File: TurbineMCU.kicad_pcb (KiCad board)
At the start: 4 copper layers, 53.7 x 54.7 mm, 44 parts, among them IC1 MSPM0G3507SPMR, IC2 TPS73533DRVT, J1 Conn_01x02_Socket, J10 Conn_01x03_Socket, J13 Conn_01x03_Socket, J14 Conn_01x03_Socket, J15 Conn_01x08_Pin, J2 Conn_01x02_Socket, J3 Conn_01x04_Socket, J5 Conn_01x03_Socket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

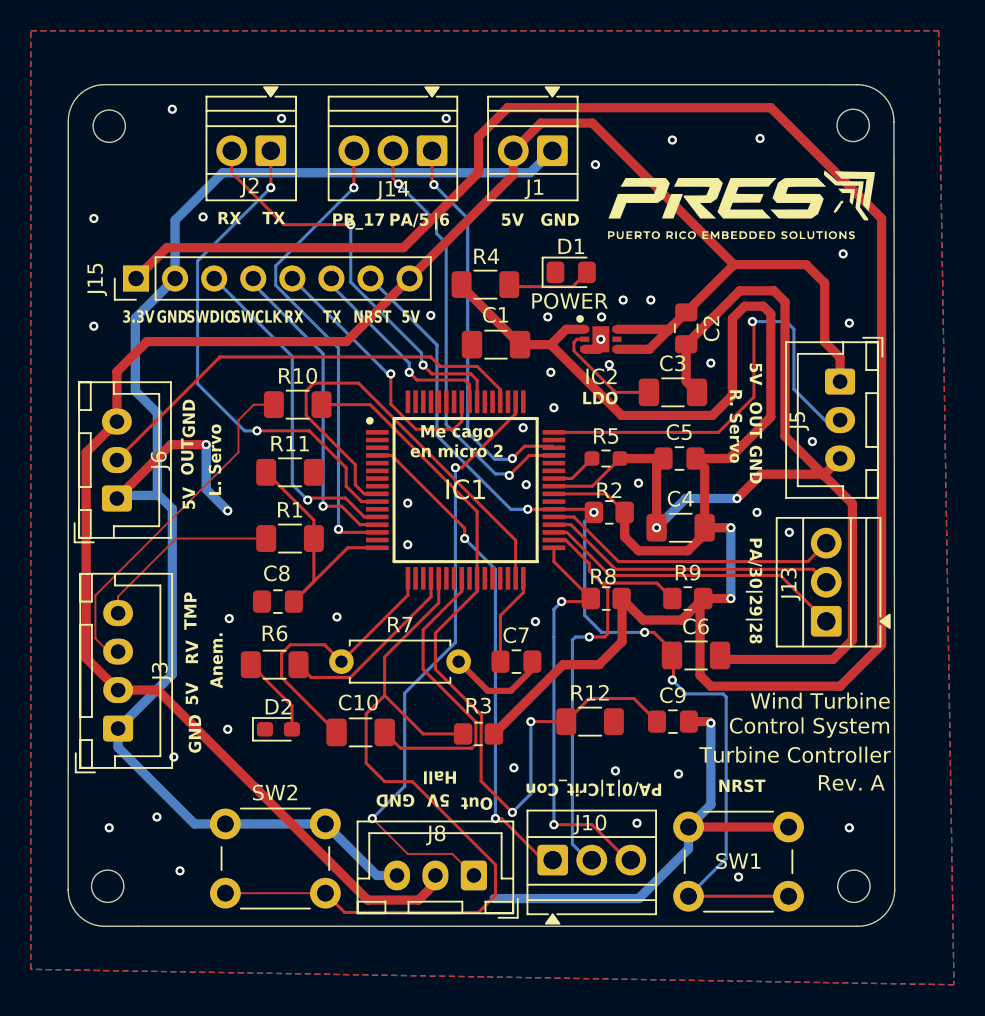
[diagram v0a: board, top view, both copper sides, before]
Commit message: Improved LDO layout based on manufacturer guidelines
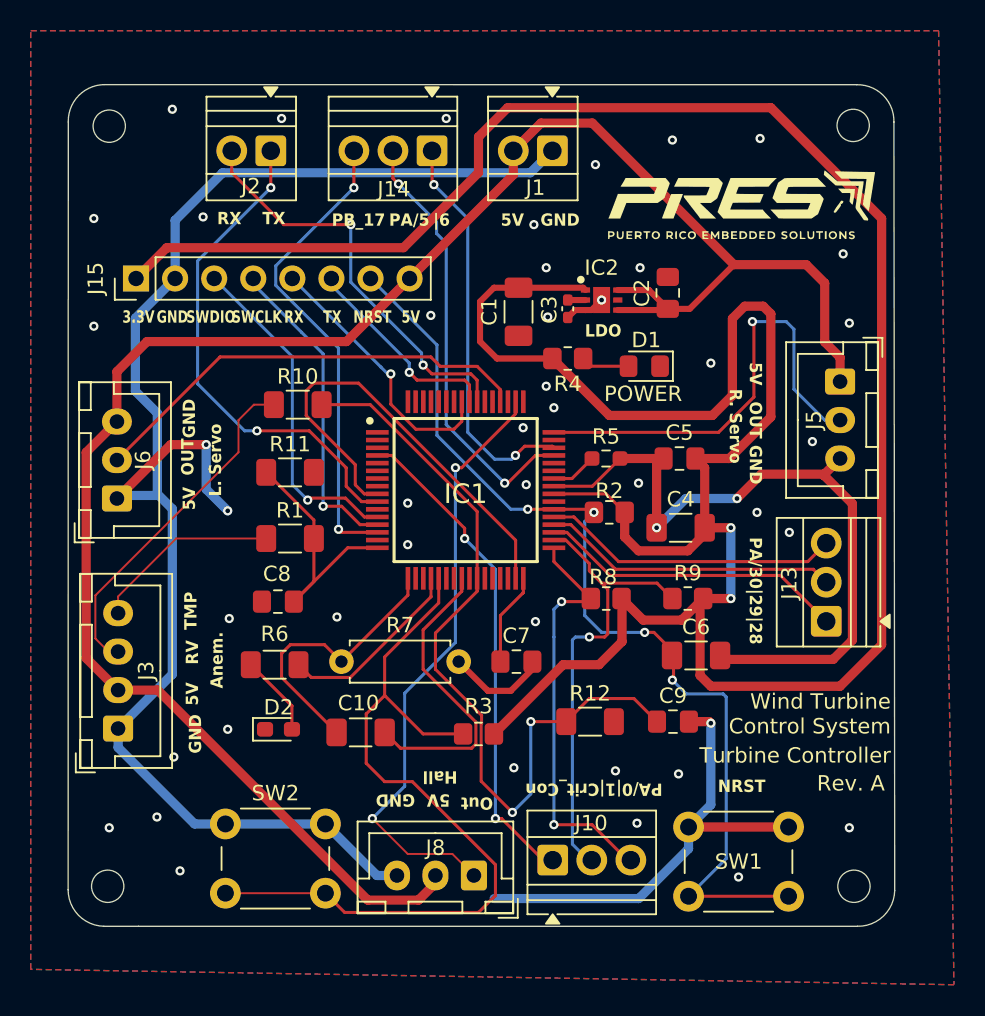
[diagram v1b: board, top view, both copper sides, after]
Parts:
- C3: footprint Capacitor_SMD:C_1206_3216Metric_Pad1.33x1.80mm_HandSolder -> Capacitor_SMD:C_0402_1005Metric_Pad0.74x0.62mm_HandSolder
- R4: footprint Resistor_SMD:R_1206_3216Metric_Pad1.30x1.75mm_HandSolder -> Resistor_SMD:R_0805_2012Metric_Pad1.20x1.40mm_HandSolder
- moved C3 8.73 mm to (177.9, 80.1), turned to -90 degrees
- moved D1 7.73 mm to (182.9, 83.8), turned to 180 degrees
- moved R4 7.19 mm to (177.9, 83.3)
- moved C2 2.59 mm to (184.4, 79.0), turned to 90 degrees
- moved C1 2.59 mm to (174.7, 80.3), turned to -90 degrees
- moved IC2 2.55 mm to (180.1, 79.5)
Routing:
- net GND: track 211.5 -> 188.2 mm, vias 48 -> 47
- net Net-(IC2-NR): track 7.33 -> 1.15 mm
- net +3.3V: track 193.8 -> 198.2 mm
- net Net-(D1-A): track 5.49 -> 3.16 mm
- net +5V: track 128.0 -> 126.9 mm
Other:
- board text removed: "Me cago en micro 2"

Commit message: final layout
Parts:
- added G***: LOGO, LOGO, F.Cu at (171.3, 92.0)
- C10: footprint Capacitor_SMD:C_1206_3216Metric_Pad1.33x1.80mm_HandSolder -> Capacitor_SMD:C_0402_1005Metric_Pad0.74x0.62mm_HandSolder
- R7: footprint Resistor_THT:R_Axial_DIN0207_L6.3mm_D2.5mm_P7.62mm_Horizontal -> Resistor_SMD:R_0402_1005Metric_Pad0.72x0.64mm_HandSolder
- moved R7 4.55 mm to (166.1, 99.5), turned to 180 degrees
- moved C10 3.94 mm to (166.3, 104.2)
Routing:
- net Net-(IC1-PA23_VREF+): track 20.4 -> 8.82 mm
- net GND: track 188.2 -> 192.8 mm, vias 47 -> 70
- net Net-(IC1-PB22): track 52.4 -> 54.4 mm, vias 0 -> 2
- net Net-(IC1-PA21_/_A1_7_/_VREF-): track 19.0 -> 19.7 mm
- net Anemometer_RV: track 52.0 -> 51.4 mm
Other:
- board text removed: "C10"

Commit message: board finished
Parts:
- moved G*** 0.10 mm to (171.3, 92.1)
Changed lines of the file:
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@@
 	(footprint "LOGO"
 		(layer "F.Cu")
-		(at 171.262 92)
+		(at 171.262 92.1)
 		(property "Reference" "G***"
 			(at 0 0 0)

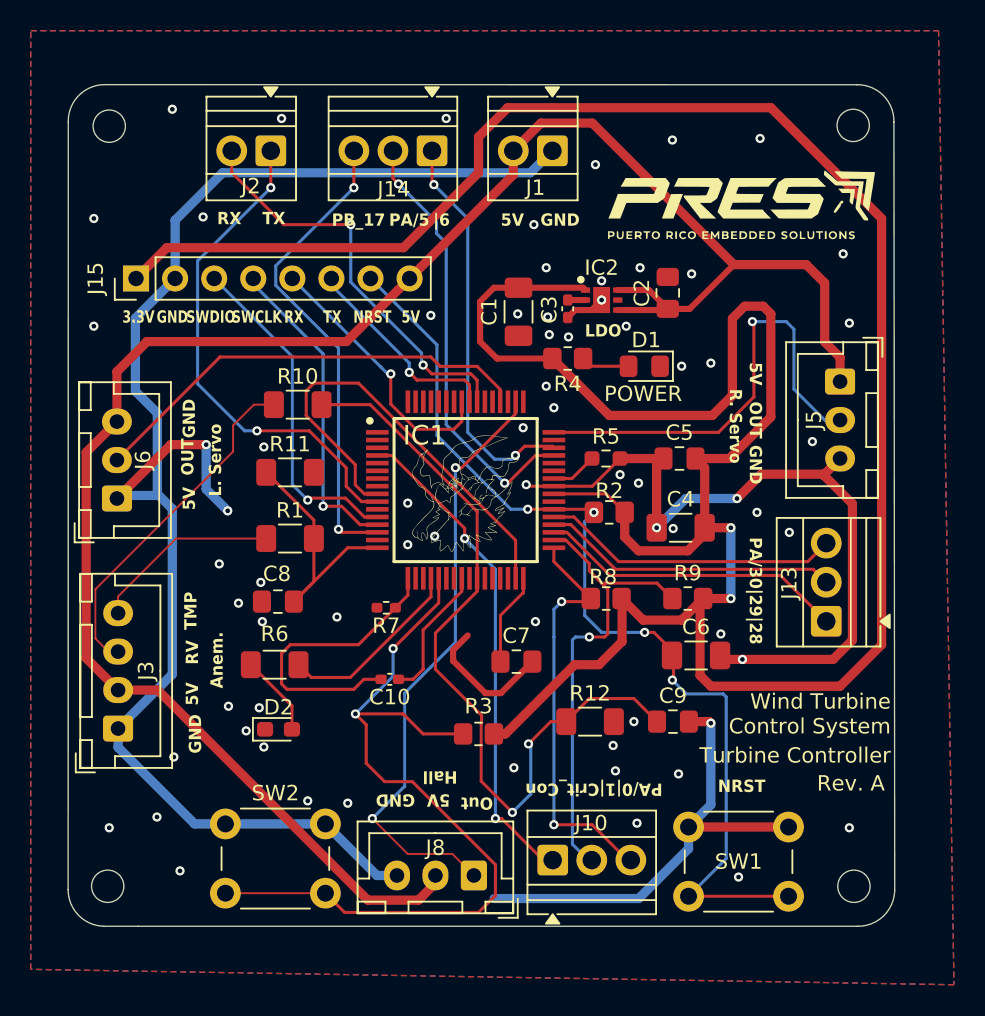
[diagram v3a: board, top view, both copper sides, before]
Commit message: Added testpoints
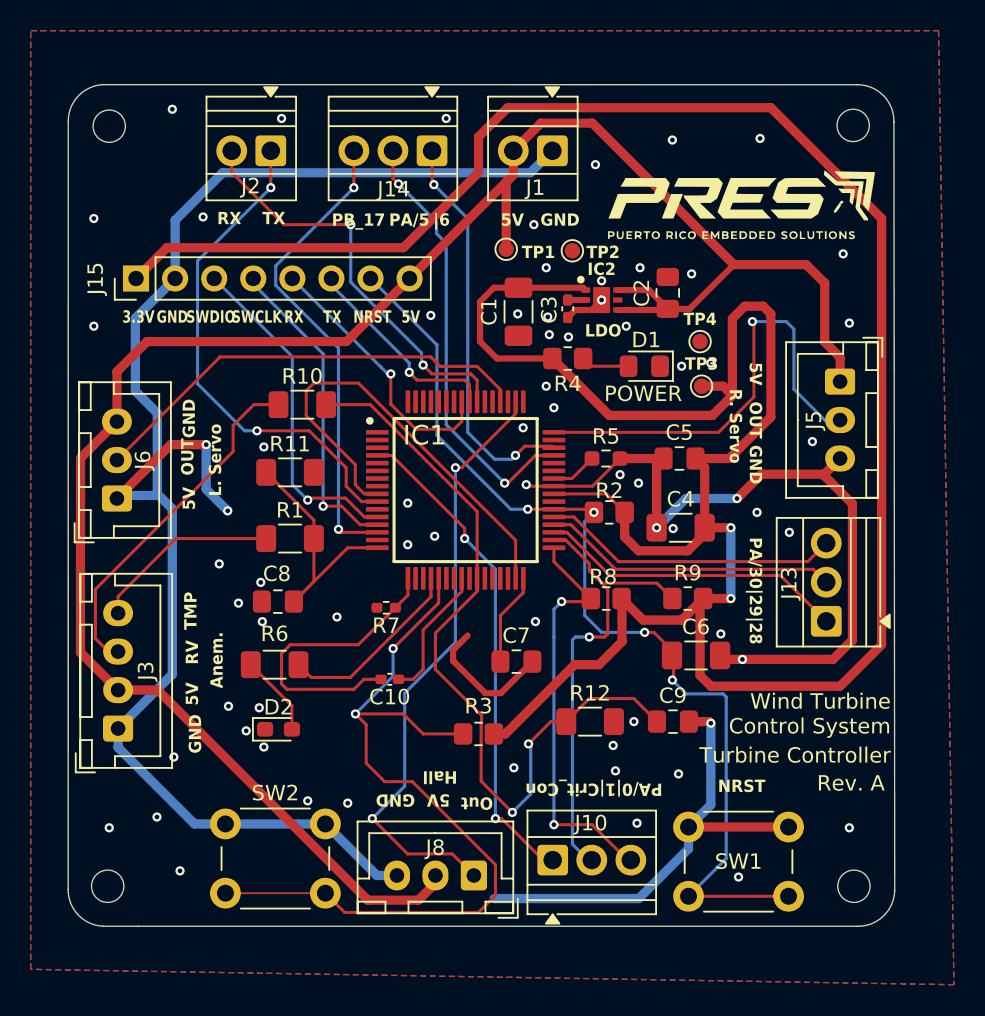
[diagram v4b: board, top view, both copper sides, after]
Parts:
- removed the G*** at (171.3, 92.1)
- added TP1: TestPoint, TestPoint:TestPoint_Pad_D1.0mm, F.Cu at (173.9, 76.2)
- added TP2: TestPoint, TestPoint:TestPoint_Pad_D1.0mm, F.Cu at (178.2, 76.3)
- added TP3: TestPoint, TestPoint:TestPoint_Pad_D1.0mm, F.Cu at (186.6, 85.1)
- added TP4: TestPoint, TestPoint:TestPoint_Pad_D1.0mm, F.Cu at (186.5, 82.2)
- moved R10 0.30 mm to (160.7, 86.3)
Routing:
- net +5V: track 126.9 -> 132.2 mm
- net +3.3V: track 198.2 -> 200.5 mm
- net Anemometer_RV: track 51.4 -> 50.7 mm

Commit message: ready for manufacturing
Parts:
- added G***: LOGO, LOGO, F.Cu at (171.3, 91.8)
- moved R12 25.5 mm to (155.2, 98.6), turned to 90 degrees
- moved C9 23.0 mm to (162.9, 99.7)
- moved R6 0.35 mm to (158.8, 103.5)
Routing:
- net Anemometer_RV: track 50.7 -> 37.0 mm, vias 2 -> 0
- net GND: track 192.8 -> 184.0 mm, vias 70 -> 68
- net Net-(IC1-PA21_/_A1_7_/_VREF-): track 19.7 -> 20.7 mm

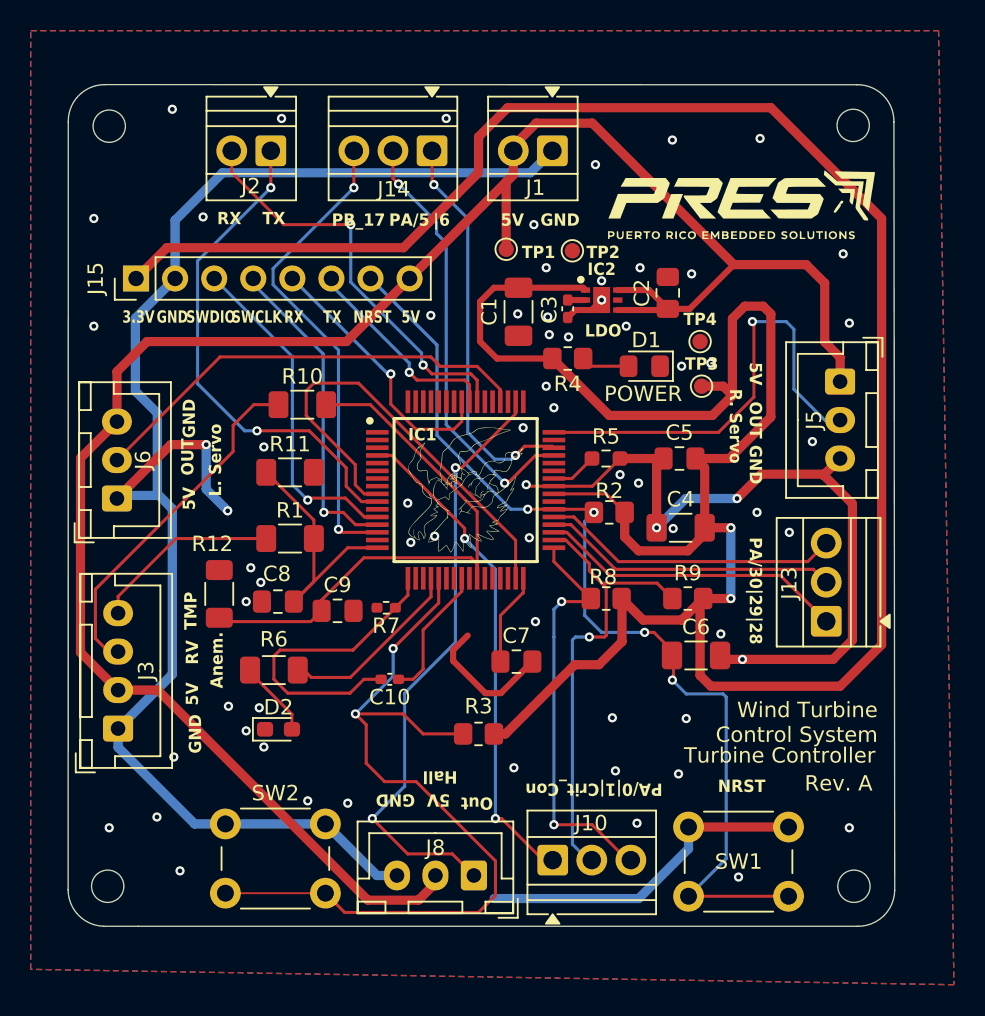
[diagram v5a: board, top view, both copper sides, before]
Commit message: Fixed silks screen
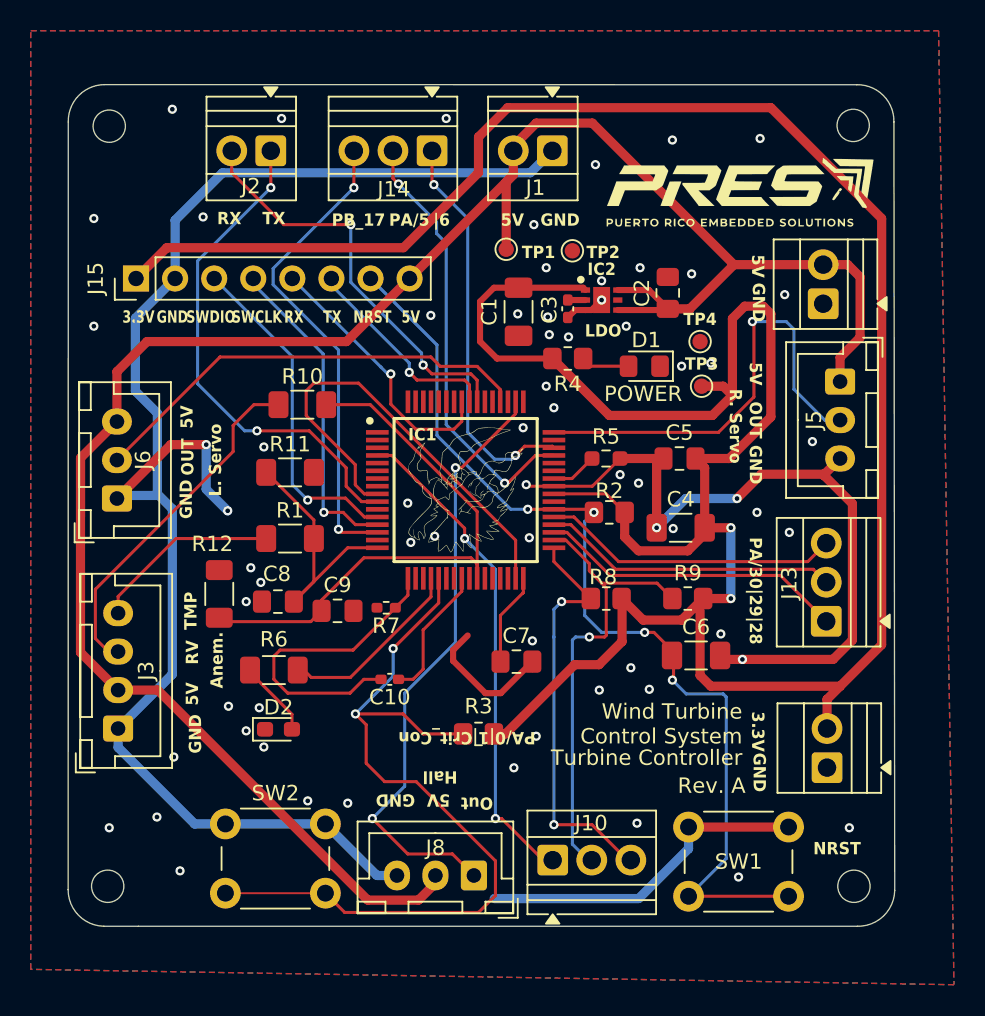
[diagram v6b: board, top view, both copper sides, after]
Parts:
- added J4: Conn_01x02_Socket, TerminalBlock:TerminalBlock_Xinya_XY308-2.54-2P_1x02_P2.54mm_Horizontal, F.Cu at (194.8, 109.9)
- added J7: Conn_01x02_Socket, TerminalBlock:TerminalBlock_Xinya_XY308-2.54-2P_1x02_P2.54mm_Horizontal, F.Cu at (194.5, 79.7)
- R8, R9: value 47k -> 4.7k
- moved G*** 0.82 mm to (188.9, 72.8)
- moved G*** 0.50 mm to (184.3, 82.3)
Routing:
- net +3.3V: track 200.5 -> 203.6 mm
- net +5V: track 132.4 -> 135.1 mm
- net GND: vias 68 -> 67
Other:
- copper layers 4 -> 2
